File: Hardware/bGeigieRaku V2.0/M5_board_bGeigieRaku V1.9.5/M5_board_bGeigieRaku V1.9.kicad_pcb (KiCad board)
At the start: 2 copper layers, 129.4 x 64.6 mm, 19 parts, among them J1 M5 2x15 pin, J10 QI GND, J11 QI charger Plus, J2 Geiger, J3 GPS, J7 Conn_01x14_Female, J8 QI charger GND, J9 QI +, SW1 SW_SPDT

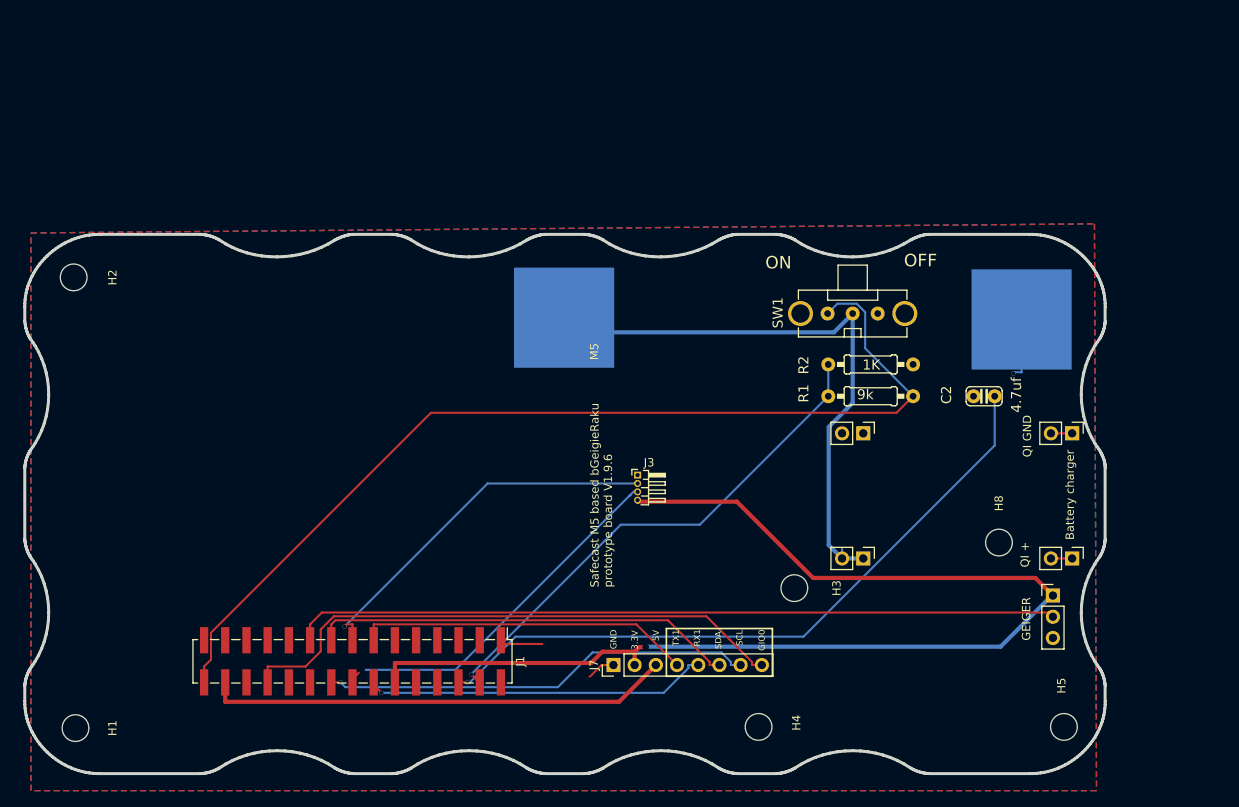
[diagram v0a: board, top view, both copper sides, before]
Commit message: Updated board. Flipped LiPo
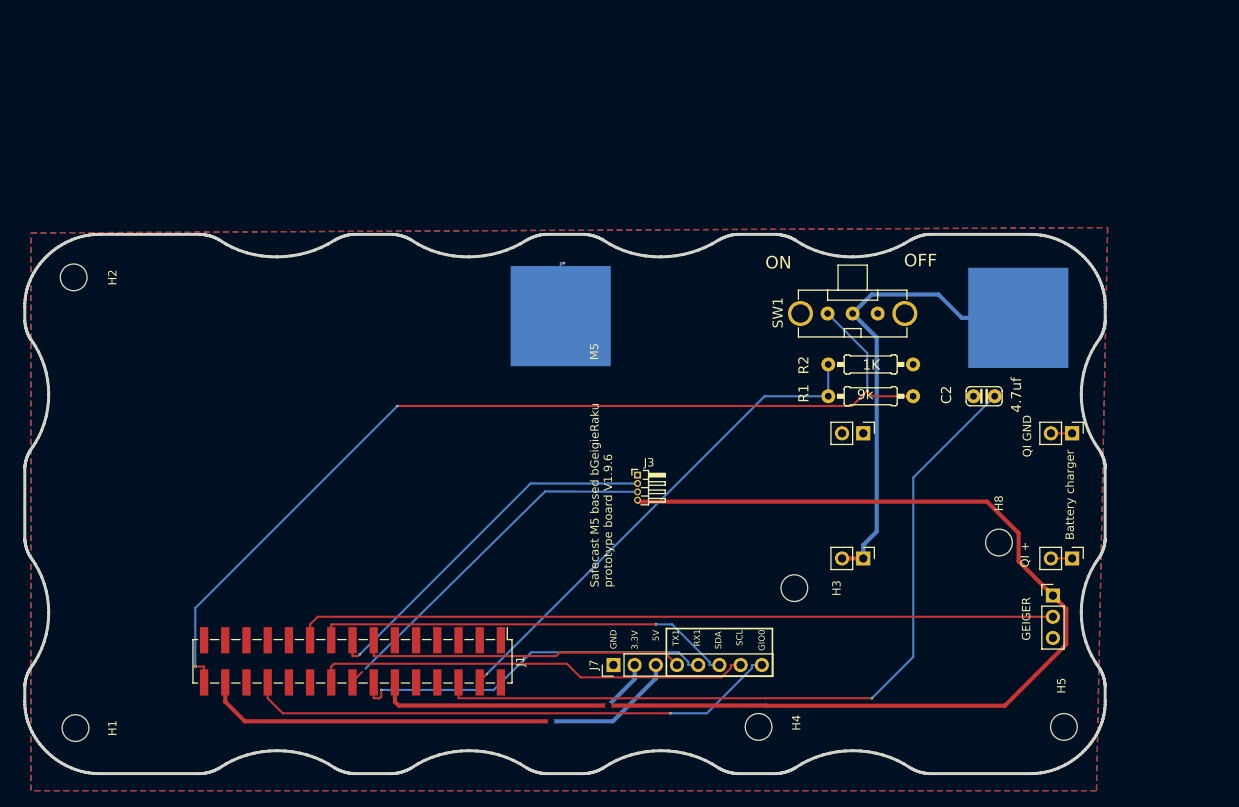
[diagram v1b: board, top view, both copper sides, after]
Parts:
- turned BT1 to 180 degrees
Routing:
- net /VBATT: track 73.7 -> 55.7 mm
- net 3.3V: track 140.6 -> 155.0 mm
- net /Reset: track 81.9 -> 93.7 mm
- net GND: track 16.5 -> 6.73 mm, vias 3 -> 1
- net /GIO0: track 67.7 -> 64.5 mm, vias 0 -> 1
- net /RX1: track 41.2 -> 44.4 mm
- net 5V: track 55.7 -> 58.6 mm, vias 0 -> 1
- net Net-(J1-Pad4): track 61.8 -> 59.8 mm
- net Net-(J1-Pad30): track 120.0 -> 118.2 mm, vias 0 -> 3
- net /TX1: track 40.3 -> 39.0 mm
- net /SCL: track 51.8 -> 52.6 mm, vias 1 -> 0
- net /TX2: track 45.2 -> 44.6 mm
- net /RX2: track 43.7 -> 43.1 mm
- net /SDA: track 51.0 -> 50.6 mm, vias 0 -> 1

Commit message: Updated board
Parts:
- added H6: MountingHole_Pad, MountingHole:MountingHole_3.2mm_M3, F.Cu at (103.6, 78.1)
- added H7: MountingHole_Pad, MountingHole:MountingHole_3.2mm_M3, F.Cu at (103.6, 122.1)
- moved H4 52.1 mm to (172.2, 73.6)
- moved H5 52.1 mm to (208.7, 73.6)
- moved BT1 45.5 mm to (175.2, 122.1)
- moved J2 14.6 mm to (207.1, 95.3)
- moved H3 14.6 mm to (176.1, 94.4)
- moved H8 14.6 mm to (200.6, 89.0)
- moved J7 6.61 mm to (158.1, 112.4)
- moved C2 4.06 mm to (199.2, 82.0)
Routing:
- net 3.3V: track 155.0 -> 112.9 mm, vias 1 -> 0
- net Net-(J1-Pad4): track 59.8 -> 73.7 mm
- net /VBATT: track 55.7 -> 68.2 mm
- net Net-(J1-Pad30): track 118.2 -> 108.5 mm, vias 3 -> 1
- net /Reset: track 93.7 -> 102.6 mm
- net /SCL: track 52.6 -> 60.8 mm, vias 0 -> 2
- net /GIO2: track 91.3 -> 96.7 mm
- net /GIO0: track 64.5 -> 69.2 mm
- net /TX1: track 39.0 -> 42.9 mm
- net /SDA: track 50.6 -> 53.7 mm, vias 1 -> 0
- net /RX2: track 43.1 -> 45.8 mm
- net /RX1: track 44.4 -> 46.5 mm
- net /TX2: track 44.6 -> 43.2 mm
- net 5V: track 58.6 -> 59.2 mm

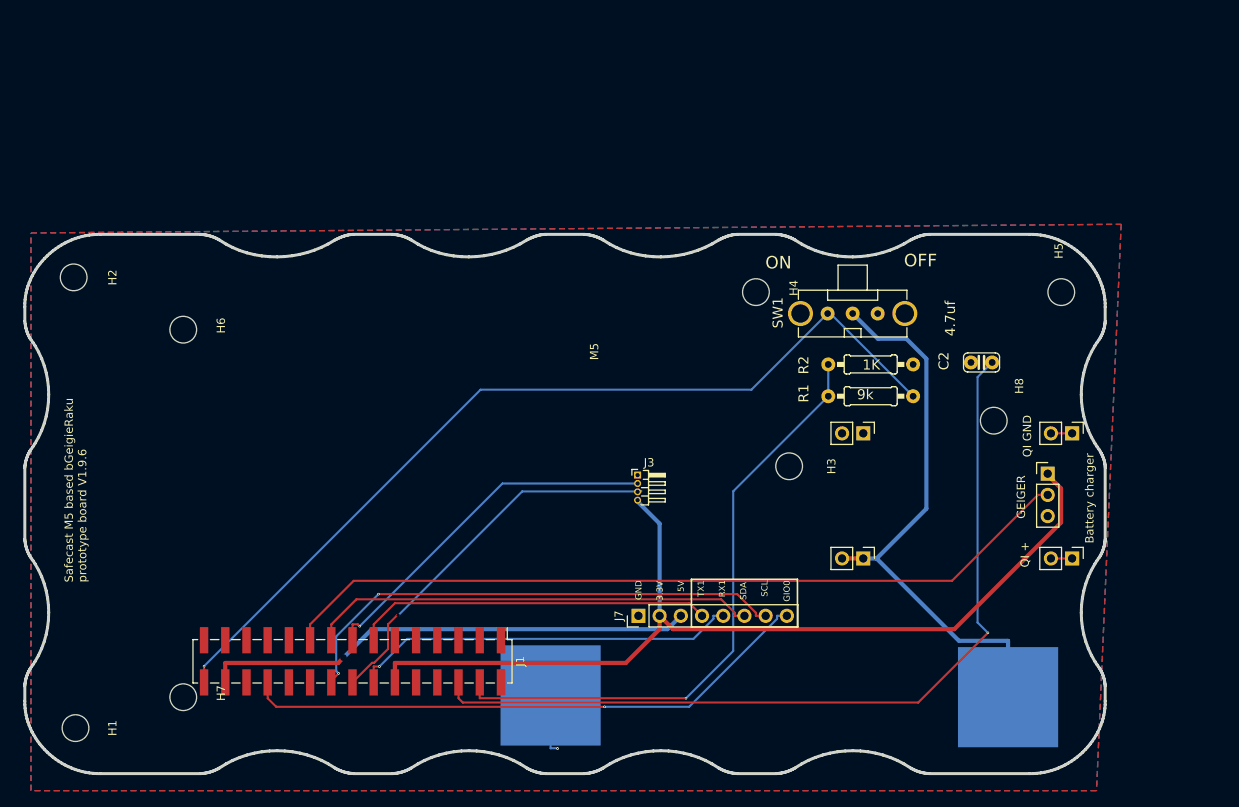
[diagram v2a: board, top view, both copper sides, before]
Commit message: Updated board for BN-880Q
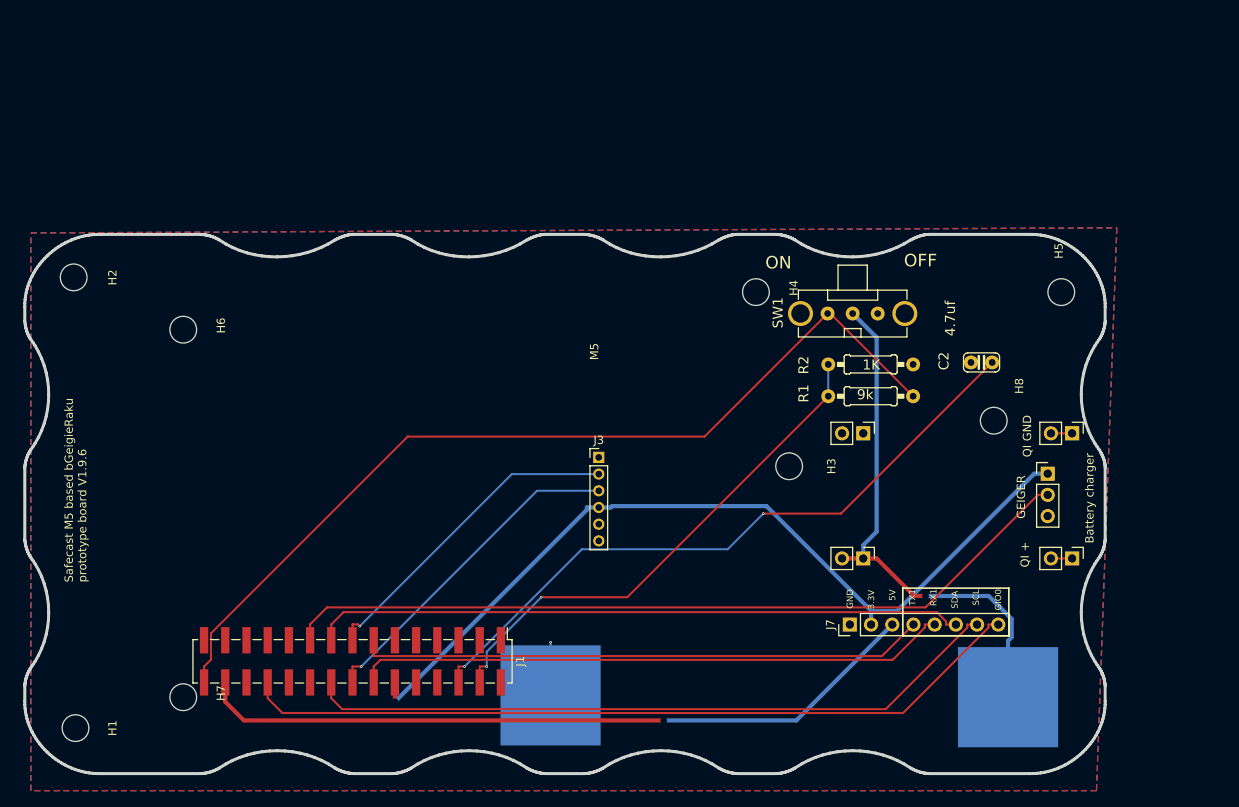
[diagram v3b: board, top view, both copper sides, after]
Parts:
- J3: footprint Connector_PinHeader_1.00mm:PinHeader_1x04_P1.00mm_Horizontal -> Connector_PinHeader_2.00mm:PinHeader_1x06_P2.00mm_Vertical
- moved J7 25.3 mm to (183.4, 113.4)
- moved J3 5.11 mm to (153.3, 93.4)
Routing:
- net 5V: track 59.2 -> 87.9 mm
- net /GIO0: track 69.2 -> 94.8 mm, vias 1 -> 0
- net /TX1: track 42.9 -> 68.1 mm
- net /RX1: track 46.5 -> 71.4 mm, vias 1 -> 0
- net /SDA: track 53.7 -> 78.2 mm
- net /SCL: track 60.8 -> 84.2 mm, vias 2 -> 0
- net /Reset: track 102.6 -> 80.9 mm, vias 1 -> 2
- net Net-(J1-Pad4): track 73.7 -> 61.9 mm, vias 1 -> 2
- net 3.3V: track 112.9 -> 104.1 mm, vias 0 -> 1
- net /RX2: track 45.8 -> 40.1 mm
- net /TX2: track 43.2 -> 39.0 mm
- net /VBATT: track 68.2 -> 64.1 mm, vias 0 -> 1
- net Net-(J1-Pad30): track 108.5 -> 110.3 mm, vias 1 -> 0
- net GND: track 7.18 -> 6.37 mm

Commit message: Updated board V1.9.6
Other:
- board text added: "Safecast bGeigieZen board V1.9.6"
- board text removed: "M5"
- board text removed: "Safecast M5 based bGeigieRaku prototype board V1.9.6"
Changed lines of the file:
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@@
     )
     (model "${KISYS3DMOD}/Misc.3dshapes/lnd7318-2.wrl"
-      (offset (xyz -18.5 -3.5 -6.5))
+      (offset (xyz -18.5 -3.5 -10.5))
       (scale (xyz 4 4 4))
       (rotate (xyz 90 0 -150))
@@
       (offset (xyz -6 6.5 -10))
       (scale (xyz 1 1 1))
+      (rotate (xyz 0 0 0))
+    )
+    (model "/home/rob/Documents/Freecad/irover board only.step"
+      (offset (xyz -17 4 -17))
+      (scale (xyz 1 1 1))
+      (rotate (xyz 0 -180 -90))
+    )
+    (model "${KISYSMOD}/packages3d/hex-spacers-m3-m-f.3dshapes/hexagonal_spacer_MF_M3_H10_HEX5.5_FTD6_MTL6.step"
+      (offset (xyz -6 6 -16))
+      (scale (xyz 1 1 0.4))
+      (rotate (xyz 0 0 0))
+    )
+    (model "${KISYSMOD}/packages3d/hex-spacers-m3-m-f.3dshapes/hexagonal_spacer_MF_M3_H10_HEX5.5_FTD6_MTL6.step"
+      (offset (xyz -30 0.5 -16))
+      (scale (xyz 1 1 0.4))
       (rotate (xyz 0 0 0))
     )
@@
     )
     (model "${KIPRJMOD}/shapes3D/KEYELCO_54.wrl"
-      (offset (xyz -27.5 0 2))
+      (offset (xyz -27.5 0 1.5))
       (scale (xyz 1 1 1))
       (rotate (xyz -90 0 -90))
@@
     )
     (model "${KISYS3DMOD}/Battery.3dshapes/18650 Li-Ion Battery.wrl"
-      (offset (xyz 32.5 0 12.5))
+      (offset (xyz 32.5 0 10.5))
       (scale (xyz 0.9 1 0.9))
       (rotate (xyz -90 90 0))
@@
     (effects (font (size 0.75 0.75) (thickness 0.15)) (justify mirror))
   )
-  (gr_text "Safecast M5 based bGeigieRaku \nprototype board V1.9.6" (at 90.7826 96.03 90) (layer "B.SilkS")
-    (effects (font (size 1 1) (thickness 0.1)) (justify mirror))
+  (gr_text "Safecast  bGeigieZen\nboard V1.9.6" (at 91.7326 98.63 90) (layer "B.SilkS")
+    (effects (font (size 2 2) (thickness 0.3)) (justify mirror))
   )
   (gr_text "TX1" (at 190.8963 110.278388 90) (layer "B.SilkS")
@@
     (effects (font (size 0.75 0.75) (thickness 0.15)) (justify mirror))
   )
-  (gr_text "M5" (at 163.1692 87.324 90) (layer "B.SilkS")
-    (effects (font (size 1 1) (thickness 0.15)) (justify mirror))
-  )
   (gr_text "GIO0" (at 201.1833 110.4331 90) (layer "B.SilkS")
     (effects (font (size 0.75 0.75) (thickness 0.15)) (justify mirror))
@@
     (effects (font (size 1 1) (thickness 0.15)))
   )
+  (gr_text "Safecast  bGeigieZen \nboard V1.9.6" (at 91.6776 96.605 90) (layer "F.SilkS")
+    (effects (font (size 2 2) (thickness 0.3)))
+  )
   (gr_text "SDA" (at 195.9763 110.4331 90) (layer "F.SilkS")
     (effects (font (size 0.75 0.75) (thickness 0.15)))
@@
     (effects (font (size 0.75 0.75) (thickness 0.15)))
   )
-  (gr_text "Safecast M5 based bGeigieRaku \nprototype board V1.9.6\n\n" (at 91.4826 108.355 90) (layer "F.SilkS")
-    (effects (font (size 1 1) (thickness 0.1)) (justify left))
-  )
-  (gr_text "M5" (at 152.8076 80.705 90) (layer "F.SilkS")
-    (effects (font (size 1 1) (thickness 0.15)))
-  )
   (dimension (type aligned) (layer "Dwgs.User")

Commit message: Tested SafePulse layout
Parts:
- added J4: Geiger, Connector_PinHeader_2.54mm:PinHeader_1x03_P2.54mm_Vertical, F.Cu at (197.7, 76.7)
- J9: value QI + -> QI Plus
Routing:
- net 3.3V: track 104.1 -> 129.1 mm
- net /GIO2: track 96.7 -> 118.3 mm, vias 0 -> 2
- net /SCL: track 84.2 -> 88.3 mm, vias 0 -> 1
- net /Reset: track 80.9 -> 84.7 mm
- net 5V: track 87.9 -> 87.7 mm, vias 1 -> 0
- net /RX1: vias 0 -> 1

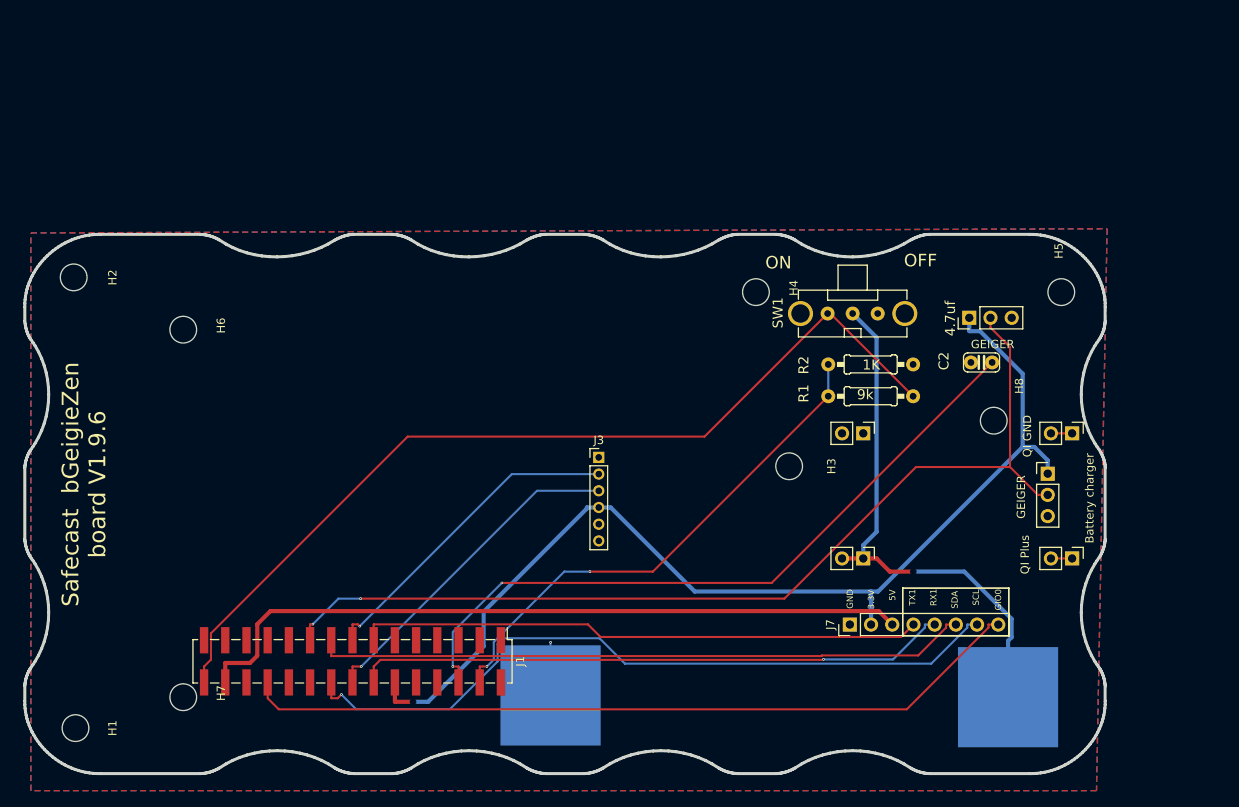
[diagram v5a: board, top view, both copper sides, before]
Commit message: Added display error on no SDcard
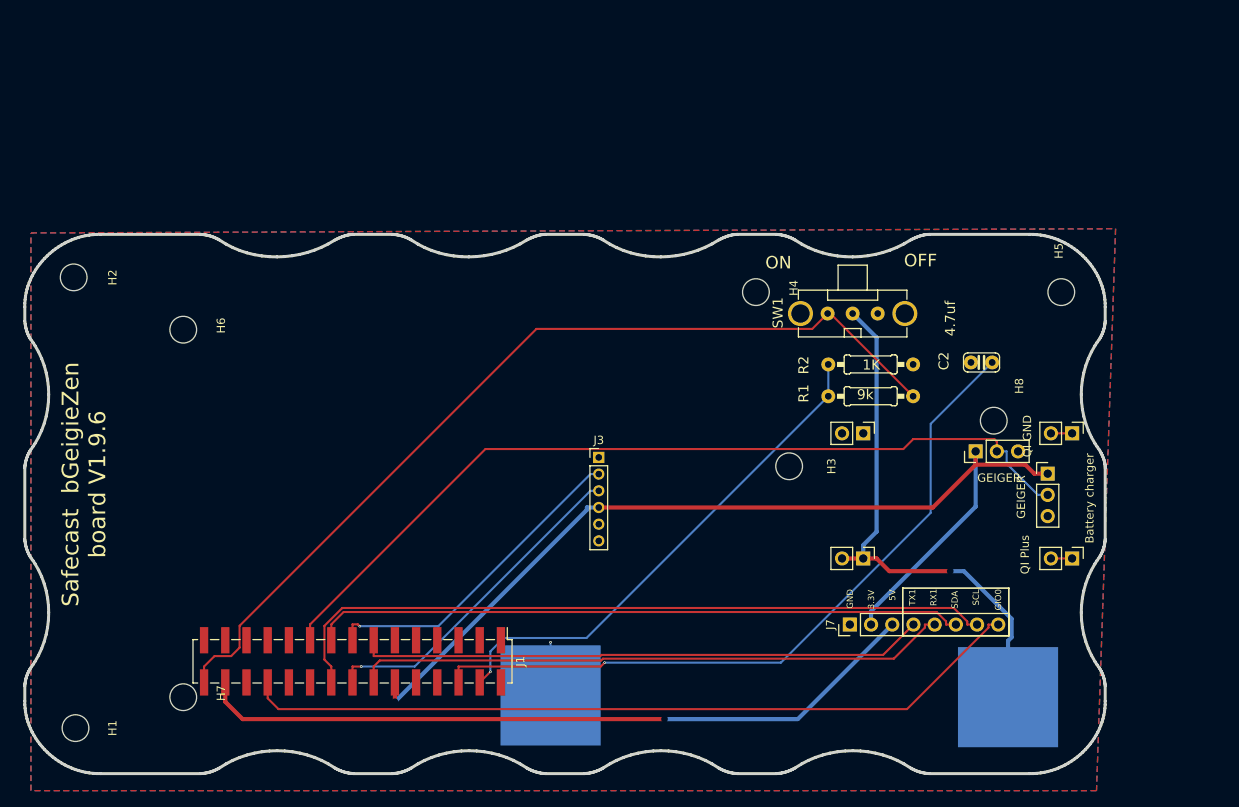
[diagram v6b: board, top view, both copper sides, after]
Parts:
- moved J4 16.0 mm to (198.5, 92.7)
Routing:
- net /GIO2: track 118.3 -> 103.8 mm, vias 2 -> 0
- net 3.3V: track 129.1 -> 120.4 mm
- net /Reset: track 84.7 -> 87.1 mm, vias 2 -> 1
- net /SCL: track 88.3 -> 87.2 mm, vias 1 -> 0
- net Net-(J1-Pad4): track 62.1 -> 61.2 mm, vias 2 -> 1
- net 5V: track 87.7 -> 87.8 mm, vias 0 -> 1
- net /RX1: vias 1 -> 0

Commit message: added P channel MOSFET for protection.
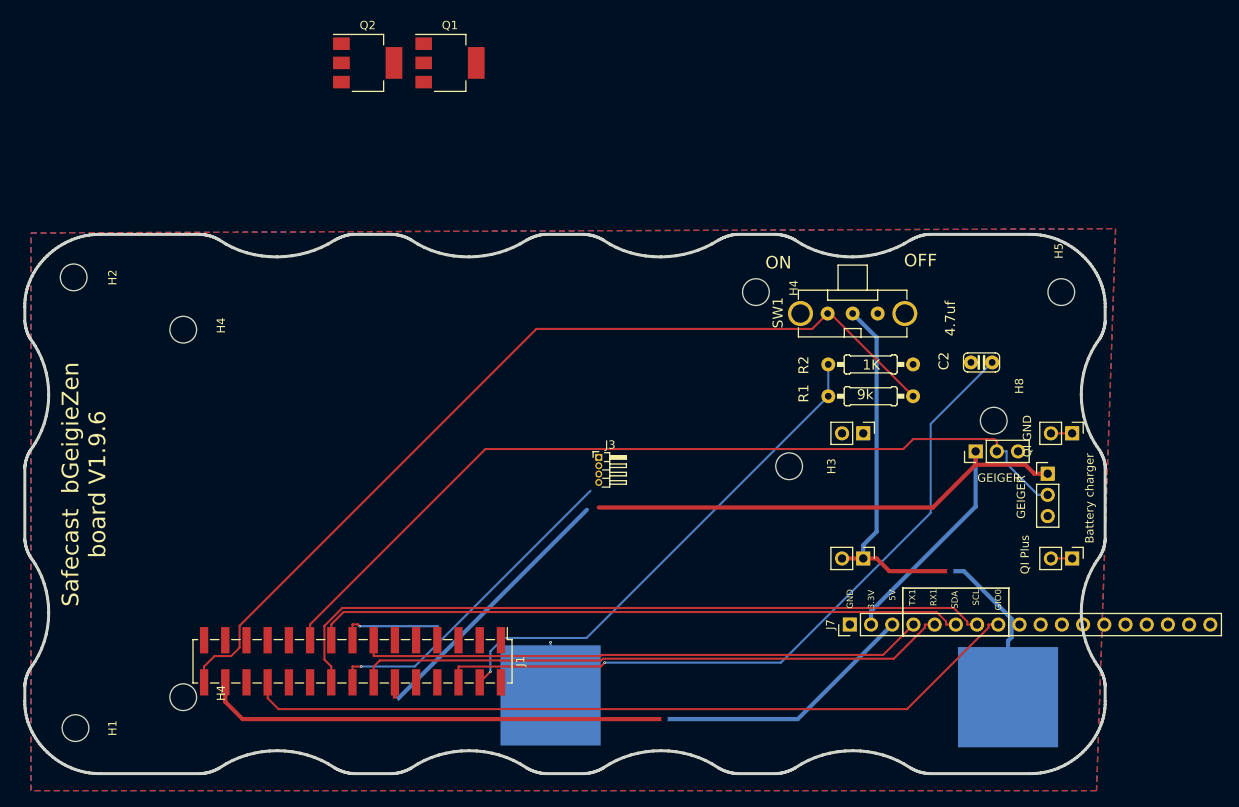
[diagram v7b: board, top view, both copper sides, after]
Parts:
- added Q1: ZXMP4A16G, Package_TO_SOT_SMD:SOT-223-3_TabPin2, F.Cu at (135.5, 46.1)
- added Q2: ZXMP4A16G, Package_TO_SOT_SMD:SOT-223-3_TabPin2, F.Cu at (125.7, 46.1)
- J3: footprint Connector_PinHeader_2.00mm:PinHeader_1x06_P2.00mm_Vertical -> Connector_PinHeader_1.00mm:PinHeader_1x04_P1.00mm_Horizontal
- J7: footprint Connector_PinHeader_2.54mm:PinHeader_1x08_P2.54mm_Vertical -> Connector_PinHeader_2.54mm:PinHeader_1x18_P2.54mm_Vertical
- renumbered H6 to H4, H7 to H4, J4 to J2
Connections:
- BT1 pad 1: /VBATT -> Net-(BT1-Pad1)
- H1 pad 1: Net-(H1-Pad1) -> unconnected-(H1-Pad1)
- H2 pad 1: Net-(H2-Pad1) -> unconnected-(H2-Pad1)
- H3 pad 1: Net-(H3-Pad1) -> unconnected-(H3-Pad1)
- H4 pad 1: Net-(H4-Pad1) -> unconnected-(H4-Pad1) (x3)
- H5 pad 1: Net-(H5-Pad1) -> unconnected-(H5-Pad1)
- H8 pad 1: Net-(H8-Pad1) -> unconnected-(H8-Pad1)
- J1 pad 10: Net-(J1-Pad10) -> unconnected-(J1-Pad10)
- J1 pad 11: Net-(J1-Pad11) -> unconnected-(J1-Pad11)
- J1 pad 21: Net-(J1-Pad21) -> unconnected-(J1-Pad21)
- J1 pad 23: Net-(J1-Pad23) -> unconnected-(J1-Pad23)
- J1 pad 25: Net-(J1-Pad25) -> unconnected-(J1-Pad25)
- J1 pad 27: Net-(J1-Pad27) -> unconnected-(J1-Pad27)
- J1 pad 29: Net-(J1-Pad29) -> unconnected-(J1-Pad29)
- J1 pad 7: Net-(J1-Pad7) -> unconnected-(J1-Pad7)
- J1 pad 8: Net-(J1-Pad8) -> unconnected-(J1-Pad8)
- J1 pad 9: Net-(J1-Pad9) -> unconnected-(J1-Pad9)
- J8 pad 2: GND -> Net-(J8-Pad2)
- SW1 pad 1: Net-(SW1-Pad1) -> unconnected-(SW1-Pad1)
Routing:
- net /TX2: track 39.0 -> 12.3 mm
- net 3.3V: track 120.4 -> 118.7 mm
- net /RX2: track 40.1 -> 39.1 mm
